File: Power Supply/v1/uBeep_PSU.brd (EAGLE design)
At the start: 160 x 100 mm, 1 part, among them U1 RAC10-12DK/277

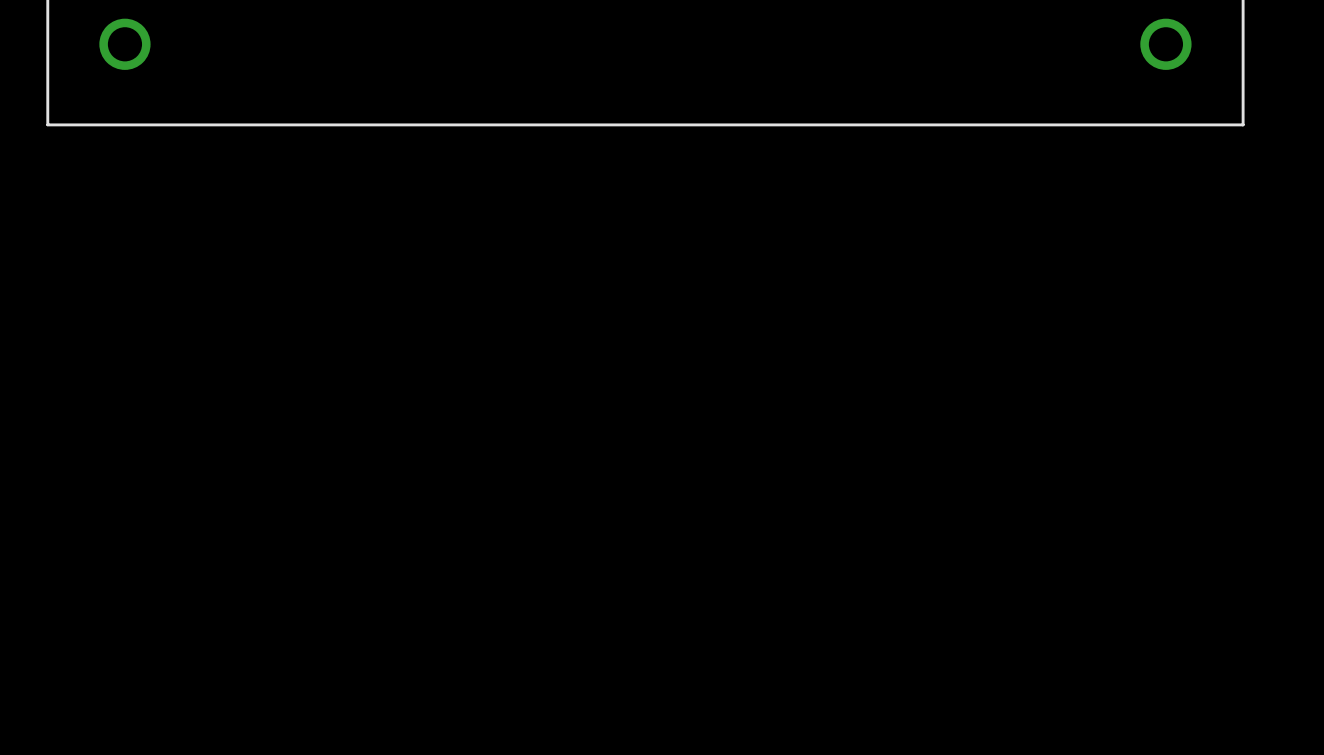
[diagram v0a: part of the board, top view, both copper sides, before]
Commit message: Added AC input
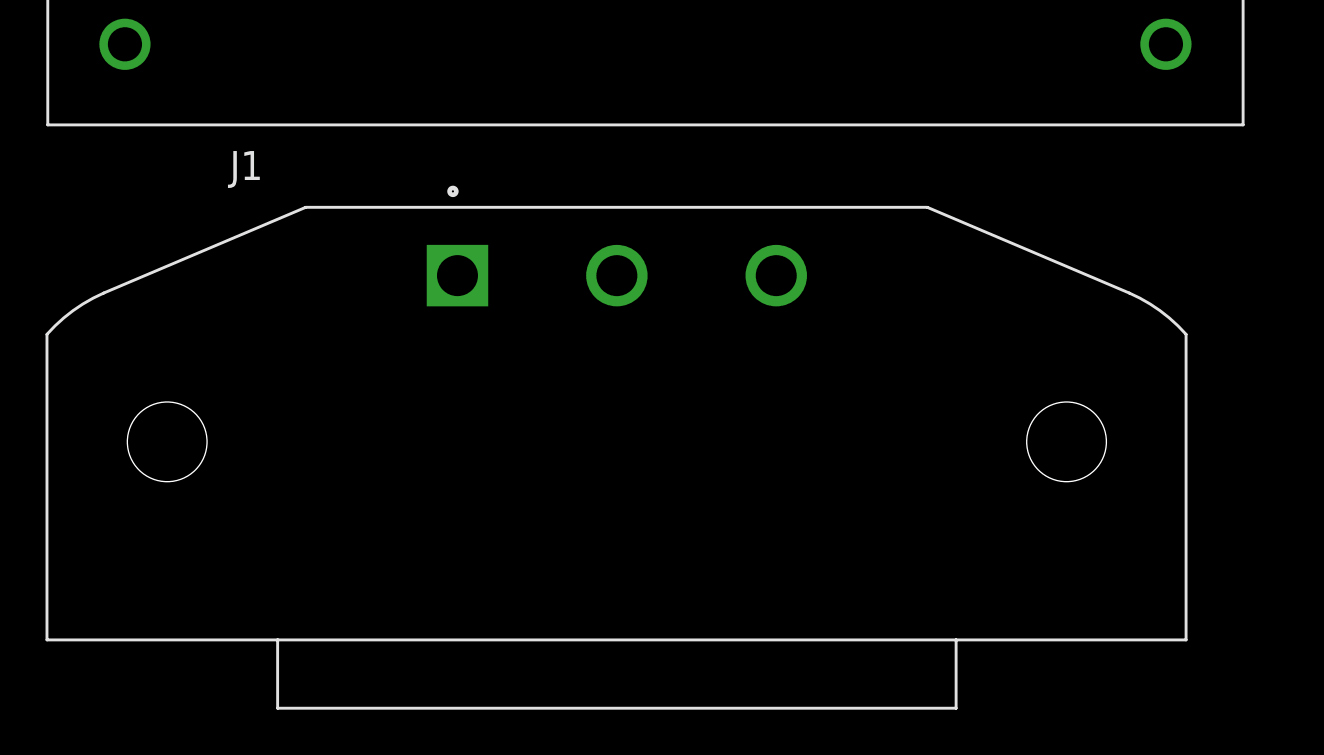
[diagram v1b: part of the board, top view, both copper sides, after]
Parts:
- added J1: 703W-00/52, roomready:703W-00/52
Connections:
- new net AC_E: J1.E
- net AC_N: now also J1.N
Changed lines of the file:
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@@
 <attribute name="NAME" x="-65.659" y="27.94" size="1.27" layer="25"/>
+</element>
+<element name="J1" library="roomready" library_urn="urn:adsk.eagle:library:9911636" package="703W-00/52" package3d_urn="urn:adsk.eagle:package:12502137/10" value="703W-00/52" x="-40.64" y="-6.35" smashed="yes">
+<attribute name="NAME" x="-57.625" y="-2.15" size="1.2725" layer="25"/>
 </element>
 </elements>
@@
 <signal name="AC_N">
 <contactref element="U1" pad="P$1"/>
+<contactref element="J1" pad="N"/>
+<wire x1="-33.625" y1="-6.35" x2="-62.23" y2="24.13" width="0" layer="19" extent="1-1"/>
+</signal>
+<signal name="AC_E">
+<contactref element="J1" pad="E"/>
 </signal>
 </signals>

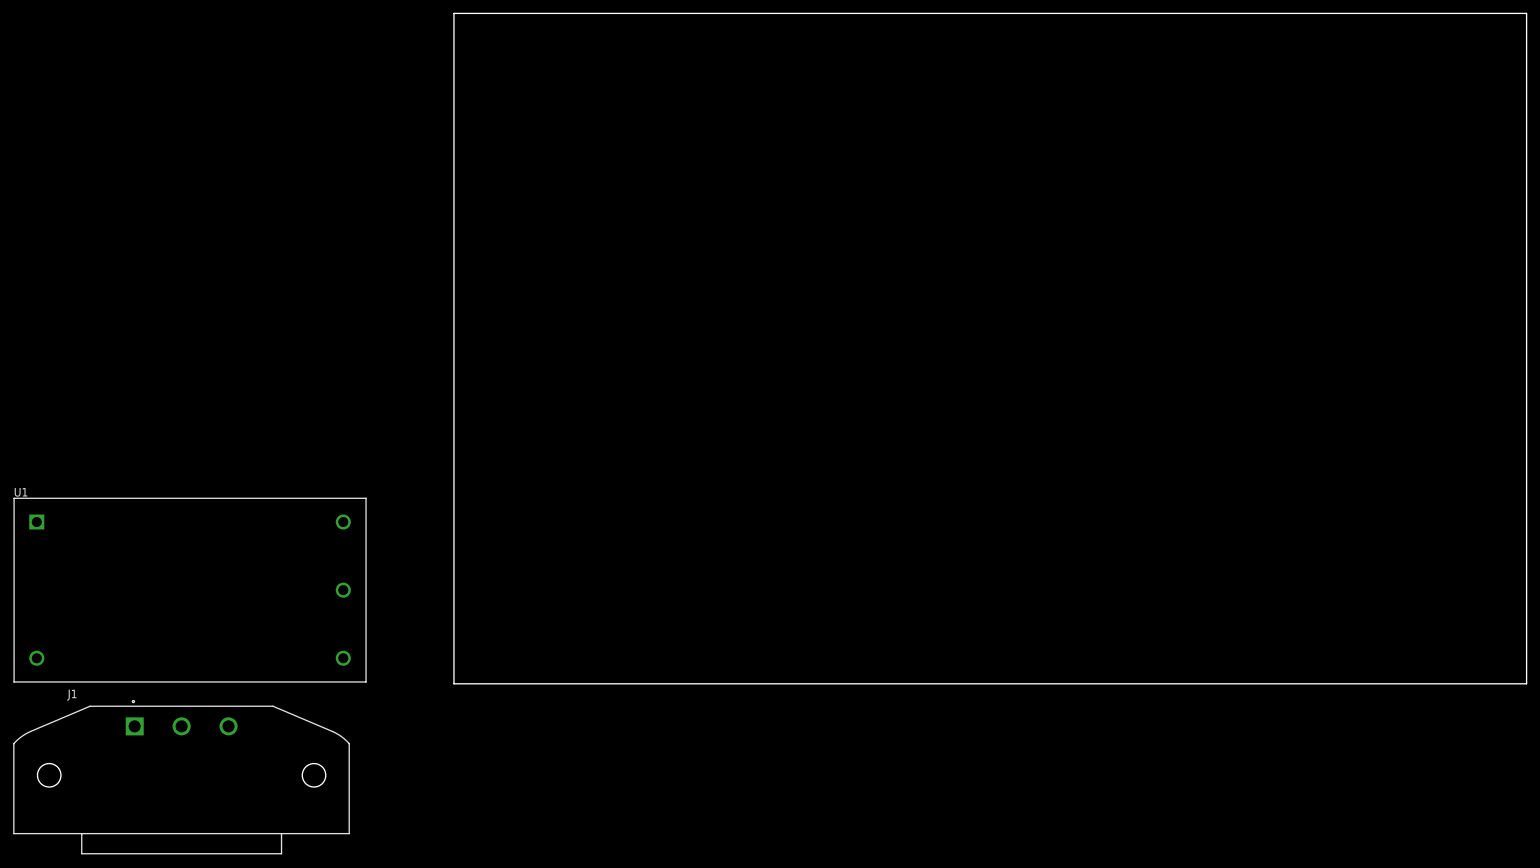
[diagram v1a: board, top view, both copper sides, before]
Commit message: Add fuse holder
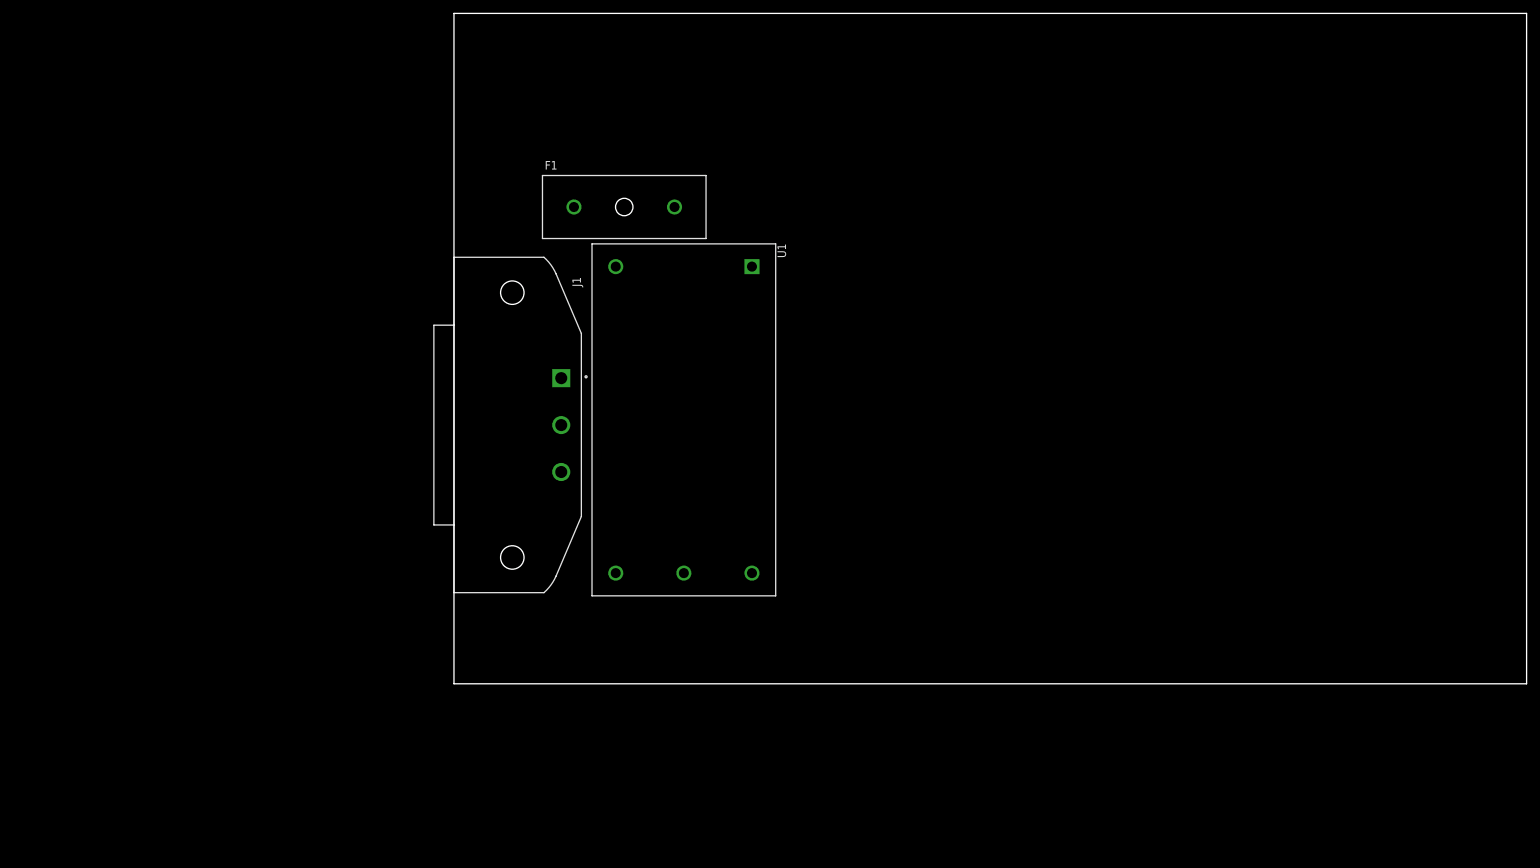
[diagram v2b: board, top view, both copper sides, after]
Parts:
- added F1: (no value), roomready:0PTF0075P
- moved U1 77.9 mm to (34.3, 39.4), turned to 270 degrees
- moved J1 72.3 mm to (16.0, 38.6), turned to 270 degrees
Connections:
- new net N$1: F1.1, J1.L
- net AC_L: now also F1.2
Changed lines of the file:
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@@
 </autorouter>
 <elements>
-<element name="U1" library="roomready" library_urn="urn:adsk.eagle:library:9911636" package="RAC10-DK/277" package3d_urn="urn:adsk.eagle:package:12501210/3" value="RAC10-12DK/277" x="-39.37" y="13.97" smashed="yes">
-<attribute name="NAME" x="-65.659" y="27.94" size="1.27" layer="25"/>
+<element name="U1" library="roomready" library_urn="urn:adsk.eagle:library:9911636" package="RAC10-DK/277" package3d_urn="urn:adsk.eagle:package:12501210/3" value="RAC10-12DK/277" x="34.29" y="39.37" smashed="yes" rot="R270">
+<attribute name="NAME" x="48.26" y="65.659" size="1.27" layer="25" rot="R270"/>
 </element>
-<element name="J1" library="roomready" library_urn="urn:adsk.eagle:library:9911636" package="703W-00/52" package3d_urn="urn:adsk.eagle:package:12502137/10" value="703W-00/52" x="-40.64" y="-6.35" smashed="yes">
-<attribute name="NAME" x="-57.625" y="-2.15" size="1.2725" layer="25"/>
+<element name="J1" library="roomready" library_urn="urn:adsk.eagle:library:9911636" package="703W-00/52" package3d_urn="urn:adsk.eagle:package:12502137/10" value="703W-00/52" x="16.002" y="38.608" smashed="yes" rot="R270">
+<attribute name="NAME" x="17.662" y="60.673" size="1.2725" layer="25" rot="R270"/>
+</element>
+<element name="F1" library="roomready" library_urn="urn:adsk.eagle:library:9911636" package="0PTF0075P" package3d_urn="urn:adsk.eagle:package:7587831/2" value="" x="25.4" y="71.12" smashed="yes">
+<attribute name="NAME" x="13.533" y="76.708" size="1.27" layer="25"/>
 </element>
 </elements>
@@
 <signal name="AC_L">
 <contactref element="U1" pad="P$2"/>
+<contactref element="F1" pad="2"/>
+<wire x1="24.13" y1="62.23" x2="32.9" y2="71.12" width="0" layer="19" extent="1-1"/>
 </signal>
 <signal name="AC_N">
 <contactref element="U1" pad="P$1"/>
 <contactref element="J1" pad="N"/>
-<wire x1="-33.625" y1="-6.35" x2="-62.23" y2="24.13" width="0" layer="19" extent="1-1"/>
+<wire x1="16.002" y1="31.593" x2="44.45" y2="62.23" width="0" layer="19" extent="1-1"/>
 </signal>
 <signal name="AC_E">
 <contactref element="J1" pad="E"/>
 </signal>
+<signal name="N$1">
+<contactref element="J1" pad="L"/>
+<contactref element="F1" pad="1"/>
+<wire x1="16.002" y1="45.593" x2="17.9" y2="71.12" width="0" layer="19" extent="1-1"/>
+</signal>
 </signals>
